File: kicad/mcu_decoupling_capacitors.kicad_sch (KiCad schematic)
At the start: 10 parts

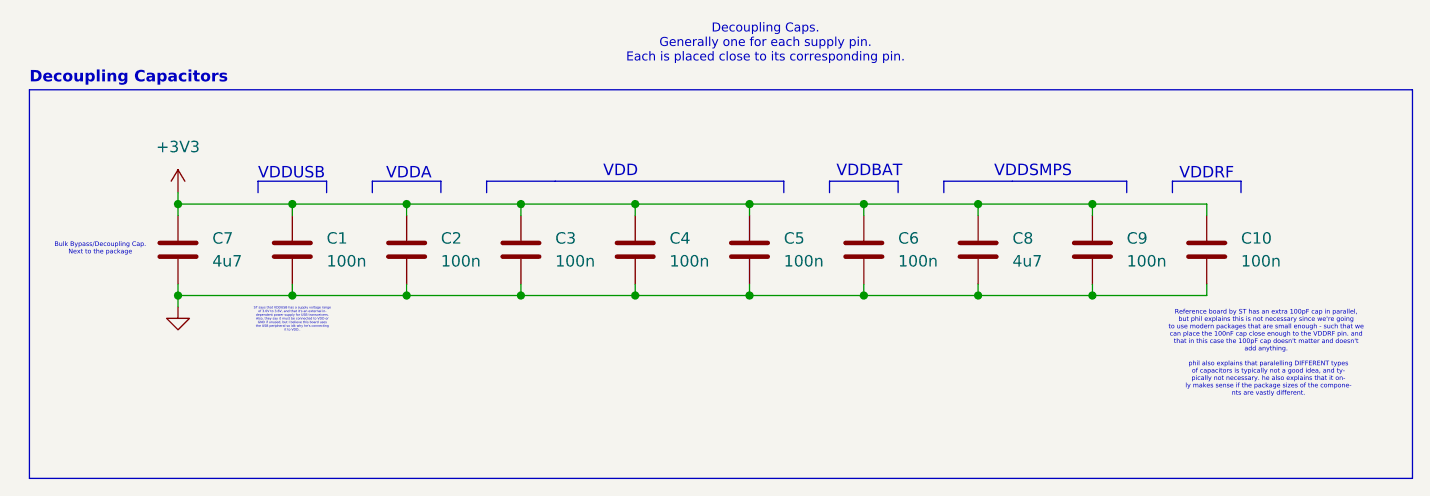
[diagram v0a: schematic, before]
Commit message: refactor(schematic): polish the schematic as much as possible - add new Basmala - fix netlist names almost EVERYWHERE, this is to help with net classes, and to help with building a good habit of naming nets properly - add a 100n capacitor to the SWD connector power pin - update many many other things EVERYWHERE
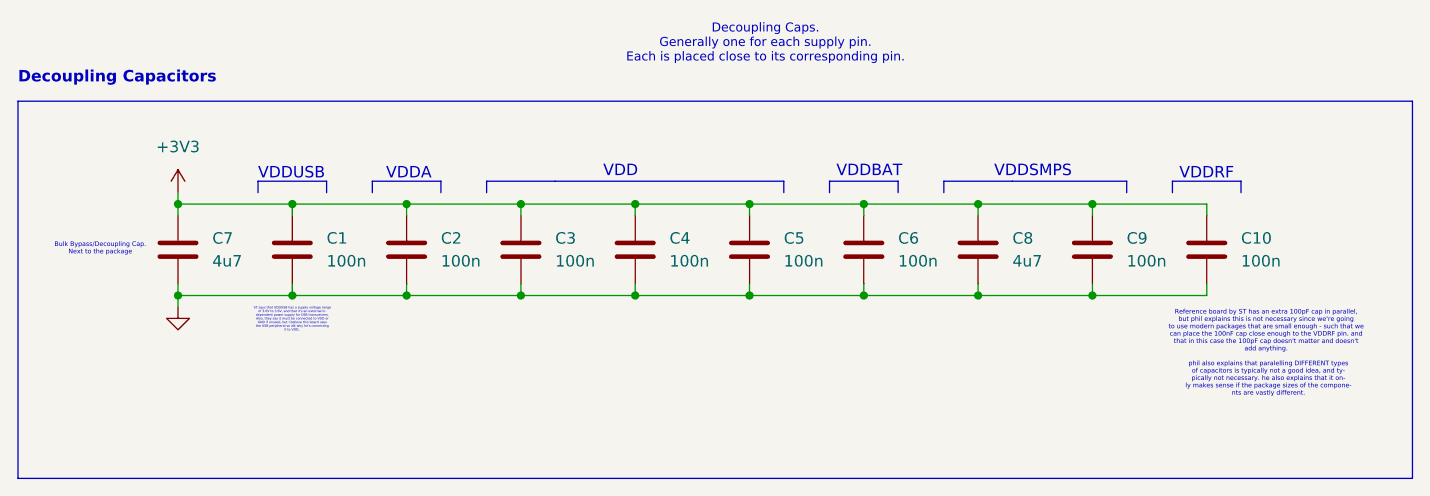
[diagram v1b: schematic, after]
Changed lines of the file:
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@@
 	)
 	(rectangle
-		(start 69.85 82.55)
+		(start 68.58 83.82)
 		(end 223.52 125.73)
 		(stroke
@@
 	(text "Decoupling Capacitors"
 		(exclude_from_sim no)
-		(at 69.85 81.28 0)
+		(at 68.58 81.28 0)
 		(effects
 			(font
